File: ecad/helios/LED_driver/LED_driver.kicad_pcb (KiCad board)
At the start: 2 copper layers, 67.2 x 100 mm, 97 parts, among them J1 Conn_02x04_Top_Bottom, J2 Conn_02x03_Top_Bottom, J3 Conn_02x04_Top_Bottom, J4 Conn_02x03_Odd_Even, Q1 IRF9Z34NPbF, Q2 PMV48XP,215, SW1 SW_Push, U1 UA9637, U2 TPS92512, U3 TPS92512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

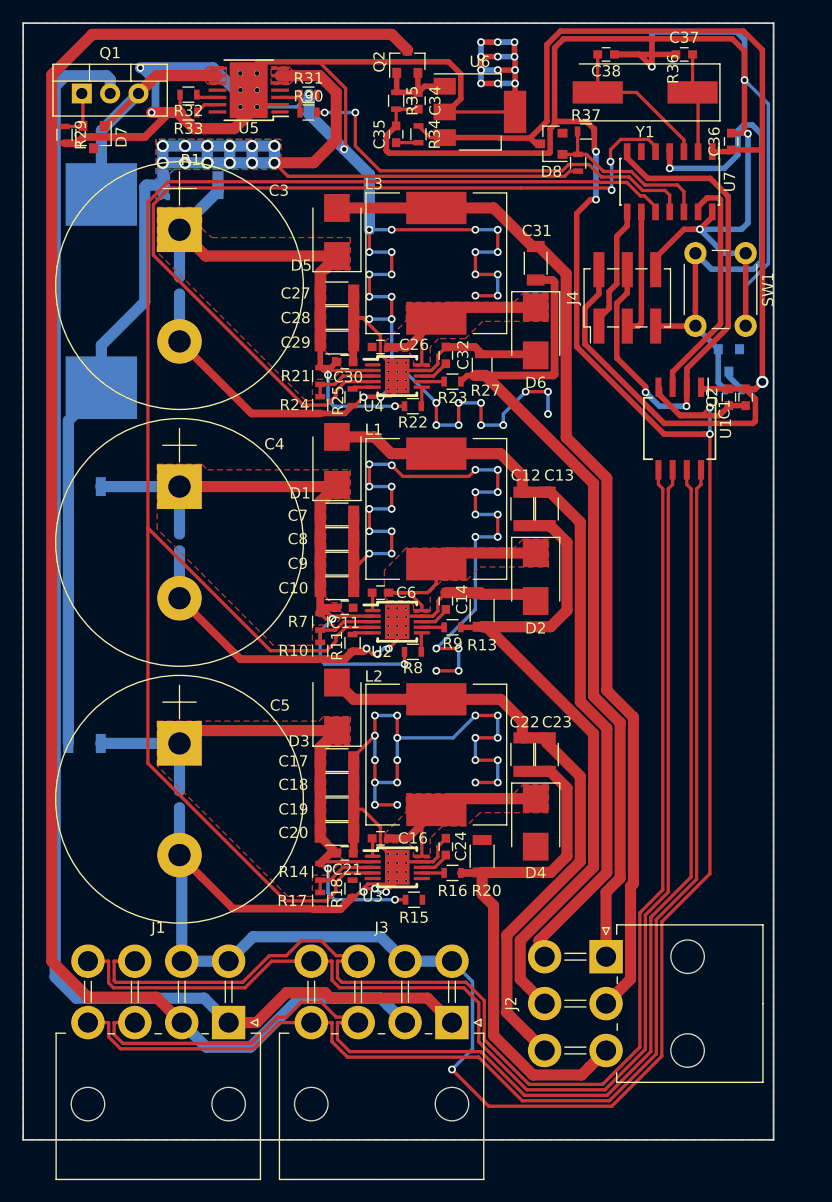
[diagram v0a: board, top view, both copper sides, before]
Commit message: Fixes small mistakes on the PCB
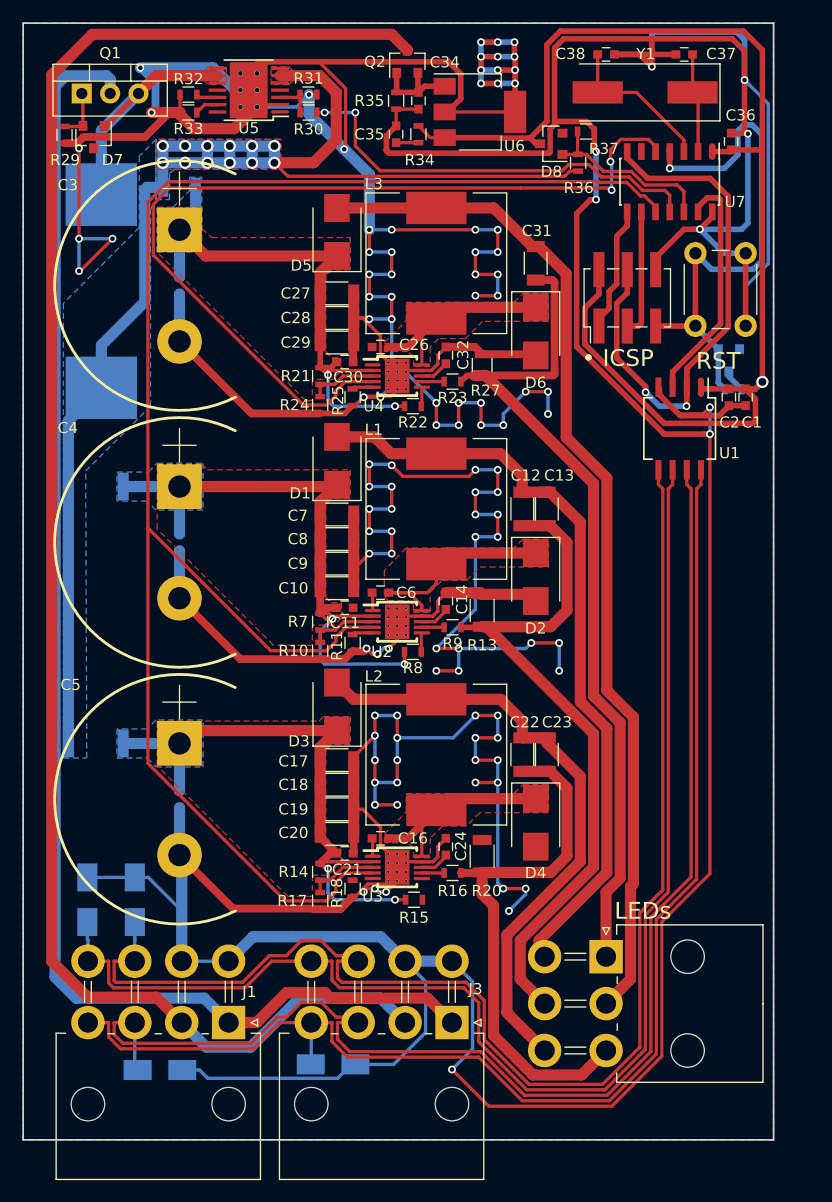
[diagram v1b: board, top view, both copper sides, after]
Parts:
- added D10: SMAJ6.0A, Diodes_SMD:D_SMA, B.Cu at (62.2, 137.2)
- added D11: SMAJ6.0A, Diodes_SMD:D_SMA, B.Cu at (77.8, 136.8)
- added D12: SMAJ6.0A, Diodes_SMD:D_SMA, B.Cu at (60.0, 122.0)
- added D13: SMAJ6.0A, Diodes_SMD:D_SMA, B.Cu at (55.8, 122.0)
- R1: value 3.3, 1W -> 15, 0.5W; footprint Resistors_SMD:R_2010 -> Resistors_SMD:R_1206
- R3, R5: value 15, 0.5W -> 3.3, 1W; footprint Resistors_SMD:R_1206 -> Resistors_SMD:R_2010
- moved R1 1.02 mm to (64.0, 58.2)
- moved R3 1.00 mm to (56.5, 85.0)
- moved R5 1.00 mm to (56.5, 108.0)
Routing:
- net GND: track 798.4 -> 889.2 mm, vias 101 -> 111
- net /DATA_-: track 119.1 -> 123.5 mm
- net /DATA_+: track 115.1 -> 118.8 mm
- net /IR_ON_+: track 115.8 -> 119.3 mm
- net /IR_ON_-: track 119.7 -> 123.2 mm
- net /Buck_Current_regulator_1.5A_2/VIN: track 55.0 -> 53.0 mm
- net /Buck_Current_regulator_1.5A_1/VIN: track 58.3 -> 56.3 mm
- net /Buck_Current_regulator_1A_1/VIN: track 55.1 -> 54.1 mm
- added copper zone on B.Cu, net /Buck_Current_regulator_1.5A_1/VIN
- added copper zone on B.Cu, net /Buck_Current_regulator_1.5A_2/VIN
- added copper zone on B.Cu, net /Buck_Current_regulator_1A_1/VIN
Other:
- board text added: "LEDs"
- board text added: "RST"
- board text added: "• ICSP"

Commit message: Improves the layout
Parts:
- added R12: 100, Resistors_SMD:R_0603, F.Cu at (110.8, 92.7)
- added REF**: MountingHole_3.2mm_M3_DIN965, Mounting_Holes:MountingHole_3.2mm_M3_DIN965, F.Cu at (53.5, 47.0)
- added REF**: MountingHole_3.2mm_M3_DIN965, Mounting_Holes:MountingHole_3.2mm_M3_DIN965, F.Cu at (116.5, 122.0)
- added REF**: MountingHole_3.2mm_M3_DIN965, Mounting_Holes:MountingHole_3.2mm_M3_DIN965, F.Cu at (116.5, 47.0)
- added REF***: OSHW-Logo2_14.6x12mm_SilkScreen, Symbols:OSHW-Logo2_14.6x12mm_SilkScreen, F.Cu at (108.0, 51.0)
- C3, C4, C5: footprint FORT:CP_Radial_D22.0mm_P10.00mm_SnapIn -> FORT:CP_Radial_D25.0mm_P10.00mm_H32mm_SnapIn
- D10, D11, D12, D13, D9, R1, R2, R3, R38, R4, R5, R6: moved to F.Cu
- J1, J3: footprint Connectors_Molex:Molex_MiniFit-JR-5569-08A2_2x04x4.20mm_Angled -> FORT:Molex_MiniFit-JR-5569-08A2_2x04x4.20mm_Angled
- J2: footprint Connectors_Molex:Molex_MiniFit-JR-5569-06A2_2x03x4.20mm_Angled -> FORT:Molex_MiniFit-JR-5569-06A2_2x03x4.20mm_Angled
- L1, L2, L3: footprint Inductors_SMD:L_Wuerth_WE-PD-Typ-LS -> FORT:7447709101
- R28: value 47, 4W -> 47, 5W; footprint FORT:R_S-5 -> Resistors_THT:R_Radial_Power_L13.0mm_W9.0mm_P5.00mm; moved to F.Cu
- Y1: footprint Crystals:Crystal_SMD_HC49-SD -> Crystals:Crystal_SMD_TXC_7M-4pin_3.2x2.5mm
- moved R31 90.9 mm to (53.4, 138.1), turned to 180 degrees
- moved Q1 90.3 mm to (73.7, 138.2), turned to 180 degrees
- moved U5 89.7 mm to (58.8, 138.5), turned to 0 degrees
- moved R32 88.2 mm to (64.2, 138.1), turned to 0 degrees
- moved R30 87.8 mm to (53.4, 136.5), turned to 180 degrees
- moved R33 85.0 mm to (64.2, 136.5), turned to 0 degrees
- moved R29 83.8 mm to (75.2, 134.5), turned to 90 degrees
- moved D7 82.2 mm to (72.7, 134.3), turned to 90 degrees
- moved J2 81.9 mm to (83.9, 47.3)
- moved Q2 73.7 mm to (111.5, 115.5), turned to 180 degrees
- moved R35 73.2 mm to (115.0, 116.5), turned to 0 degrees
- moved C35 71.9 mm to (118.0, 116.5), turned to 180 degrees
- moved C34 70.5 mm to (115.0, 114.5), turned to 0 degrees
- moved R34 69.2 mm to (118.0, 114.5), turned to 0 degrees
- moved U6 62.8 mm to (116.0, 109.0), turned to 90 degrees
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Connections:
- D10 pad 1: /DATA_- -> /IR_ON_-
- D11 pad 1: /DATA_+ -> /IR_ON_+
- D12 pad 1: /IR_ON_- -> /DATA_-
- D13 pad 1: /IR_ON_+ -> /DATA_+
- J1 pad 3: /DATA_- -> /IR_ON_-
- J1 pad 4: /DATA_+ -> /IR_ON_+
- J1 pad 7: /IR_ON_- -> /DATA_+
- J1 pad 8: /IR_ON_+ -> /DATA_-
- J2 pad 1: /VIS- -> /IRB+
- J2 pad 2: /VIS+ -> /IRA-
- J2 pad 3: /IRB- -> /IRA+
- J2 pad 4: /IRA+ -> /IRB-
- J2 pad 5: /IRA- -> /VIS+
- J2 pad 6: /IRB+ -> /VIS-
- J3 pad 3: /DATA_- -> /IR_ON_-
- J3 pad 4: /DATA_+ -> /IR_ON_+
- J3 pad 7: /IR_ON_- -> /DATA_+
- J3 pad 8: /IR_ON_+ -> /DATA_-
- J4 pad 4: /Controller/DATA_IN -> /Controller/ICSP_MOSI
- U1 pad 2: /Controller/DATA_IN -> /Controller/FLASH_IN
- U1 pad 3: /Controller/FLASH_IN -> /Controller/DATA_IN
- U1 pad 5: /IR_ON_- -> /DATA_-
- U1 pad 6: /IR_ON_+ -> /DATA_+
- U1 pad 7: /DATA_- -> /IR_ON_-
- U1 pad 8: /DATA_+ -> /IR_ON_+
- U7 pad 10: /Controller/IR_ON -> /Power_Management.sch/EN36
- U7 pad 11: /Power_Management.sch/EN36 -> /Controller/IR_ON
- U7 pad 13: /Controller/FLASH_IN -> Net-(U7-Pad13)
- U7 pad 6: Net-(U7-Pad6) -> /Controller/FLASH_IN
- U7 pad 7: /Controller/DATA_IN -> /Controller/ICSP_MOSI
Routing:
- net /Power_Management.sch/V36_PROTECTED: track 22.4 -> 137.9 mm
- net /VS6: track 150.9 -> 43.1 mm
- net /Buck_Current_regulator_1A_1/PDIM: track 81.4 -> 185.7 mm
- net /VS36: track 125.9 -> 25.5 mm
- net /IR_ON_-: track 123.2 -> 41.3 mm
- net /IR_ON_+: track 119.3 -> 47.0 mm
- net /Power_Management.sch/EN36: track 38.6 -> 107.6 mm, vias 2 -> 0
- net /DATA_-: track 123.5 -> 60.4 mm
- net /VIS+: track 91.8 -> 31.7 mm
- net /IRB-: track 48.3 -> 107.8 mm
- net /DATA_+: track 118.8 -> 61.1 mm
- net /Controller/DATA_IN: track 48.0 -> 2.60 mm, vias 2 -> 0
- net +36V: track 127.9 -> 169.7 mm, vias 12 -> 0
- net /IRB+: track 55.1 -> 94.4 mm
- net /Controller/ICSP_MOSI: track 0.00 -> 34.3 mm
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- removed copper zone on B.Cu, net +36V
- removed copper zone on B.Cu, net /Buck_Current_regulator_1.5A_1/VIN
- removed copper zone on B.Cu, net /Buck_Current_regulator_1.5A_2/VIN
- removed copper zone on B.Cu, net /Buck_Current_regulator_1A_1/VIN
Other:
- board size 67.2 x 100 mm -> 70 x 100 mm
- board text added: "FORmicidae Tracker - HELIOS - LED Driver ©2018 Alexandre Tuleu"
- board text added: "RESET"
- board text removed: "RST"

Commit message: Adds Pull-Down resistor
We do not want the LEDs to be turned ON on a UC reset.
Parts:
- added R19: 100k, Resistors_SMD:R_0603, F.Cu at (78.1, 122.6)
- added R26: 100k, Resistors_SMD:R_0603, F.Cu at (78.1, 78.2)
- moved REF*** 0.21 mm to (107.8, 50.9), turned to 90 degrees
- moved R18 0.10 mm to (79.6, 121.5)
- moved R25 0.10 mm to (79.6, 77.5)
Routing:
- net Net-(R18-Pad1): track 0.00 -> 1.76 mm
- net GND: track 906.2 -> 904.7 mm, vias 100 -> 97
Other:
- board text added: "ICSP"
- board text added: "IR+| D- IR-| D+ 06V|GND 36V|GND"
- board text added: "•"
- board text removed: "• ICSP"

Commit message: Adds a nice master board
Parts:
- removed C35: 10uF, Capacitors_SMD:C_0603
- added C15: 1uF, Capacitors_SMD:C_0603, F.Cu at (114.8, 109.1)
- added C25: 0.01uF, Capacitors_SMD:C_0603, F.Cu at (118.1, 111.8)
- added D14: UV, LEDs:LED_D5.0mm_Horizontal_O3.81mm_Z3.0mm, F.Cu at (52.0, 45.5)
- added D15: UV, LEDs:LED_D5.0mm_Horizontal_O3.81mm_Z3.0mm, F.Cu at (52.0, 139.0)
- added Q3: Q_NMOS_GSD, TO_SOT_Packages_SMD:SOT-23, F.Cu at (97.0, 46.5)
- added R39: 82, Resistors_SMD:R_0603, F.Cu at (54.5, 141.5)
- added R40: 100K, Resistors_SMD:R_0603, F.Cu at (99.5, 46.4)
- C34: value 100nF -> 1uF
- J2: footprint FORT:Molex_MiniFit-JR-5569-06A2_2x03x4.20mm_Angled -> Connectors_Molex:Molex_MiniFit-JR-5556-06A_2x03x4.20mm_Straight
- R19, R26, R29, R35, R36: value 100k -> 100K
- R3, R5: value 3.3, 1W -> 4.7, 3/4W
- R34: value 500m -> 82
- R38: value 10k -> 10K
- U6: value LM2936-5.0 -> LM3985IM5-5.0/NOPB; footprint TO_SOT_Packages_SMD:SOT-223-3Lead_TabPin2 -> TO_SOT_Packages_SMD:SOT-23-5
- Y1: value 10 MHz -> 10MHz
- moved R34 93.9 mm to (54.3, 45.5), turned to 90 degrees
- moved J2 11.0 mm to (91.7, 55.0), turned to 180 degrees
- moved R29 6.44 mm to (69.4, 137.2), turned to 180 degrees
- moved D7 6.17 mm to (69.8, 139.8), turned to 180 degrees
- moved R30 5.81 mm to (58.6, 134.0)
- moved R31 5.81 mm to (58.6, 135.6)
- moved R32 5.81 mm to (69.4, 135.6)
- moved R33 5.81 mm to (69.4, 134.0)
- moved U5 5.81 mm to (64.0, 136.0)
- moved R28 5.50 mm to (72.5, 49.0)
- moved REF** 5.00 mm to (58.5, 47.0)
- moved Q1 3.49 mm to (73.8, 134.7), turned to 270 degrees
- moved U6 2.84 mm to (115.5, 111.8)
- moved R36 0.80 mm to (104.4, 69.9)
- moved R37 0.80 mm to (105.9, 69.9)
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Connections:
- J1 pad 3: /IR_ON_- -> /IR_ON_+
- J1 pad 4: /IR_ON_+ -> /IR_ON_-
- J2 pad 1: /IRB+ -> /IRA-
- J2 pad 2: /IRA- -> /IRA+
- J2 pad 3: /IRA+ -> /VIS-
- J2 pad 5: /VIS+ -> /IRB+
- J2 pad 6: /VIS- -> /VIS+
- J3 pad 3: /IR_ON_- -> /IR_ON_+
- J3 pad 4: /IR_ON_+ -> /IR_ON_-
- R34 pad 1: +5V -> Net-(D14-Pad2)
- R34 pad 2: Net-(C35-Pad1) -> +5V
- U6 pad 3: +5V -> /Power_Management.sch/V6_PROTECTED
- U7 pad 13: Net-(U7-Pad13) -> /Controller/UV_ON
- Y1 pad 2: Net-(C38-Pad2) -> GND
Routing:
- net +5V: track 114.0 -> 297.9 mm
- net Net-(D14-Pad1): track 0.00 -> 140.5 mm
- net /Controller/UV_ON: track 0.00 -> 45.6 mm
- net /IR_ON_-: track 41.3 -> 74.5 mm
- net /IR_ON_+: track 47.0 -> 74.3 mm
- net /VS36: track 25.5 -> 47.8 mm
- net /IRB-: track 107.8 -> 89.0 mm
- net GND: track 904.7 -> 920.7 mm, vias 97 -> 103
- net /IRA-: track 71.1 -> 61.1 mm
- net /Power_Management.sch/V6_PROTECTED: track 8.12 -> 15.3 mm
- net /IRA+: track 67.1 -> 60.5 mm
- net /Power_Management.sch/EN36: track 107.6 -> 101.3 mm
- net /IRB+: track 94.4 -> 89.2 mm
- net +36V: track 169.7 -> 165.1 mm
- net /VIS-: track 47.0 -> 42.4 mm
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- removed copper zone on F.Cu, net /Power_Management.sch/V36_PROTECTED
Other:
- outline, holes or cut-outs redrawn
- board text added: "+"

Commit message: wip
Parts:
- U1: footprint Housings_SOIC:SO-8_5.3x6.2mm_Pitch1.27mm -> Housings_SOIC:SOIC-8_3.9x4.9mm_Pitch1.27mm
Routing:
- net GND: track 920.7 -> 1070.7 mm, vias 103 -> 247
- net /IR_ON_+: track 74.3 -> 75.3 mm
- net /Controller/FLASH_IN: track 30.8 -> 31.8 mm
- net /DATA_+: track 60.7 -> 61.7 mm
- net +5V: track 297.9 -> 298.9 mm

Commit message: Generates Pick and Place data for LED Driver
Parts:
- turned U2 to 0 degrees
- turned U3 to 0 degrees
- turned U4 to 0 degrees

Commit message: wip
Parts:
- Q3: value Q_NMOS_GSD -> BSS138L
- U6: value LM3985IM5-5.0/NOPB -> LP3985IM5-5.0/NOPB
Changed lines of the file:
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@@
   (general
     (links 288)
-    (no_connects 3)
+    (no_connects 6)
     (area 49.924999 43.424999 120.075001 143.575001)
     (thickness 1.6)
@@
       (effects (font (size 1 1) (thickness 0.15)))
     )
-    (fp_text value LM3985IM5-5.0/NOPB (at 0 2.9 90) (layer F.Fab)
+    (fp_text value LP3985IM5-5.0/NOPB (at 0 2.9 90) (layer F.Fab)
       (effects (font (size 1 1) (thickness 0.15)))
     )
@@
     )
   )
-  (module TO_SOT_Packages_SMD:SOT-23 (layer F.Cu)
-    (at 97 46.45 180)
-    (descr "SOT-23, Standard")
-    (tags SOT-23)
-    (attr smd)
-    (fp_text reference Q3 (at 0.8 -2.45 180) (layer F.SilkS)
-      (effects (font (size 1 1) (thickness 0.15)))
-    )
-    (fp_text value Q_NMOS_GSD (at 0 2.5 180) (layer F.Fab)
-      (effects (font (size 1 1) (thickness 0.15)))
-    )
-    (fp_text user %R (at 0 0 270) (layer F.Fab)
-      (effects (font (size 0.5 0.5) (thickness 0.075)))
-    )
-    (fp_line (start -0.7 -0.95) (end -0.7 1.5) (layer F.Fab) (width 0.1))
-    (fp_line (start -0.15 -1.52) (end 0.7 -1.52) (layer F.Fab) (width 0.1))
-    (fp_line (start -0.7 -0.95) (end -0.15 -1.52) (layer F.Fab) (width 0.1))
-    (fp_line (start 0.7 -1.52) (end 0.7 1.52) (layer F.Fab) (width 0.1))
-    (fp_line (start -0.7 1.52) (end 0.7 1.52) (layer F.Fab) (width 0.1))
-    (fp_line (start 0.76 1.58) (end 0.76 0.65) (layer F.SilkS) (width 0.12))
-    (fp_line (start 0.76 -1.58) (end 0.76 -0.65) (layer F.SilkS) (width 0.12))
-    (fp_line (start -1.7 -1.75) (end 1.7 -1.75) (layer F.CrtYd) (width 0.05))
-    (fp_line (start 1.7 -1.75) (end 1.7 1.75) (layer F.CrtYd) (width 0.05))
-    (fp_line (start 1.7 1.75) (end -1.7 1.75) (layer F.CrtYd) (width 0.05))
-    (fp_line (start -1.7 1.75) (end -1.7 -1.75) (layer F.CrtYd) (width 0.05))
-    (fp_line (start 0.76 -1.58) (end -1.4 -1.58) (layer F.SilkS) (width 0.12))
-    (fp_line (start 0.76 1.58) (end -0.7 1.58) (layer F.SilkS) (width 0.12))
-    (pad 1 smd rect (at -1 -0.95 180) (size 0.9 0.8) (layers F.Cu F.Paste F.Mask)
-      (net 66 /Controller/UV_ON))
-    (pad 2 smd rect (at -1 0.95 180) (size 0.9 0.8) (layers F.Cu F.Paste F.Mask)
-      (net 2 GND))
-    (pad 3 smd rect (at 1 0 180) (size 0.9 0.8) (layers F.Cu F.Paste F.Mask)
-      (net 63 "Net-(D14-Pad1)"))
-    (model ${KISYS3DMOD}/TO_SOT_Packages_SMD.3dshapes/SOT-23.wrl
-      (at (xyz 0 0 0))
-      (scale (xyz 1 1 1))
-      (rotate (xyz 0 0 0))
-    )
-  )
   (module Resistors_SMD:R_0603 (layer F.Cu)
     (at 54.3 45.5 90)
@@
       (at (xyz 0 0 0))
       (scale (xyz 1 1 1))
+      (rotate (xyz 0 0 0))
+    )
+  )
+  (module TO_SOT_Packages_SMD:SOT-23 (layer F.Cu)
+    (at 97 46.45 180)
+    (descr "SOT-23, Standard")
+    (tags SOT-23)
+    (attr smd)
+    (fp_text reference Q3 (at 0 -2.5 180) (layer F.SilkS)
+      (effects (font (size 1 1) (thickness 0.15)))
+    )
+    (fp_text value BSS138L (at 0 2.5 180) (layer F.Fab)
+      (effects (font (size 1 1) (thickness 0.15)))
+    )
+    (fp_text user %R (at 0 0 270) (layer F.Fab)
+      (effects (font (size 0.5 0.5) (thickness 0.075)))
+    )
+    (fp_line (start -0.7 -0.95) (end -0.7 1.5) (layer F.Fab) (width 0.1))
+    (fp_line (start -0.15 -1.52) (end 0.7 -1.52) (layer F.Fab) (width 0.1))
+    (fp_line (start -0.7 -0.95) (end -0.15 -1.52) (layer F.Fab) (width 0.1))
+    (fp_line (start 0.7 -1.52) (end 0.7 1.52) (layer F.Fab) (width 0.1))
+    (fp_line (start -0.7 1.52) (end 0.7 1.52) (layer F.Fab) (width 0.1))
+    (fp_line (start 0.76 1.58) (end 0.76 0.65) (layer F.SilkS) (width 0.12))
+    (fp_line (start 0.76 -1.58) (end 0.76 -0.65) (layer F.SilkS) (width 0.12))
+    (fp_line (start -1.7 -1.75) (end 1.7 -1.75) (layer F.CrtYd) (width 0.05))
+    (fp_line (start 1.7 -1.75) (end 1.7 1.75) (layer F.CrtYd) (width 0.05))
+    (fp_line (start 1.7 1.75) (end -1.7 1.75) (layer F.CrtYd) (width 0.05))
+    (fp_line (start -1.7 1.75) (end -1.7 -1.75) (layer F.CrtYd) (width 0.05))
+    (fp_line (start 0.76 -1.58) (end -1.4 -1.58) (layer F.SilkS) (width 0.12))
+    (fp_line (start 0.76 1.58) (end -0.7 1.58) (layer F.SilkS) (width 0.12))
+    (pad 1 smd rect (at -1 -0.95 180) (size 0.9 0.8) (layers F.Cu F.Paste F.Mask)
+      (net 66 /Controller/UV_ON))
+    (pad 2 smd rect (at -1 0.95 180) (size 0.9 0.8) (layers F.Cu F.Paste F.Mask)
+      (net 2 GND))
+    (pad 3 smd rect (at 1 0 180) (size 0.9 0.8) (layers F.Cu F.Paste F.Mask)
+      (net 63 "Net-(D14-Pad1)"))
+    (model ${KISYS3DMOD}/TO_SOT_Packages_SMD.3dshapes/SOT-23.wrl
+      (at (xyz 0 0 0))
+      (scale (xyz 1 1 1))

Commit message: wip
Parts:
- C25: value 0.01uF -> 10nF, 50V
- J4: value Conn_02x03_Odd_Even -> M20-8760342
- U5: value TPS1H100AQ -> TPS1H100AQPWPRQ1
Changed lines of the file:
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@@
   (general
     (links 288)
-    (no_connects 6)
-    (area 49.924999 43.424999 120.075001 143.575001)
+    (no_connects 3)
+    (area 37.565 36.583809 129.118572 147.605001)
     (thickness 1.6)
     (drawings 16)
@@
     (pad_to_mask_clearance 0.1)
     (aux_axis_origin 61.2 134.05)
-    (grid_origin 50 143.5)
+    (grid_origin 61.2 134.05)
     (visible_elements FFFFFFFF)
     (pcbplotparams
@@
       (viasonmask false)
       (mode 1)
-      (useauxorigin false)
+      (useauxorigin true)
       (hpglpennumber 1)
       (hpglpenspeed 20)
@@
       (effects (font (size 1 1) (thickness 0.15)))
     )
-    (fp_text value Conn_02x03_Odd_Even (at 0 4.87 90) (layer F.Fab)
+    (fp_text value M20-8760342 (at 0 4.87 90) (layer F.Fab)
       (effects (font (size 1 1) (thickness 0.15)))
     )
@@
       (effects (font (size 1 1) (thickness 0.15)))
     )
-    (fp_text value TPS1H100AQ (at 0 3.75) (layer F.Fab)
+    (fp_text value TPS1H100AQPWPRQ1 (at 0 3.75) (layer F.Fab)
       (effects (font (size 1 1) (thickness 0.15)))
     )
@@
       (effects (font (size 1 1) (thickness 0.15)))
     )
-    (fp_text value 0.01uF (at 0 1.5 270) (layer F.Fab)
+    (fp_text value "10nF, 50V" (at 0 1.5 270) (layer F.Fab)
       (effects (font (size 1 1) (thickness 0.15)))
     )
